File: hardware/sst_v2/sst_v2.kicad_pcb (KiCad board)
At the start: 4 copper layers, 60 x 90 mm, 110 parts, among them U1 Pico_2_W, U2 ADS131M04IPWR, U3 DS3231SN, Y1 ECS-2520MVLC-081.92-BN-TR

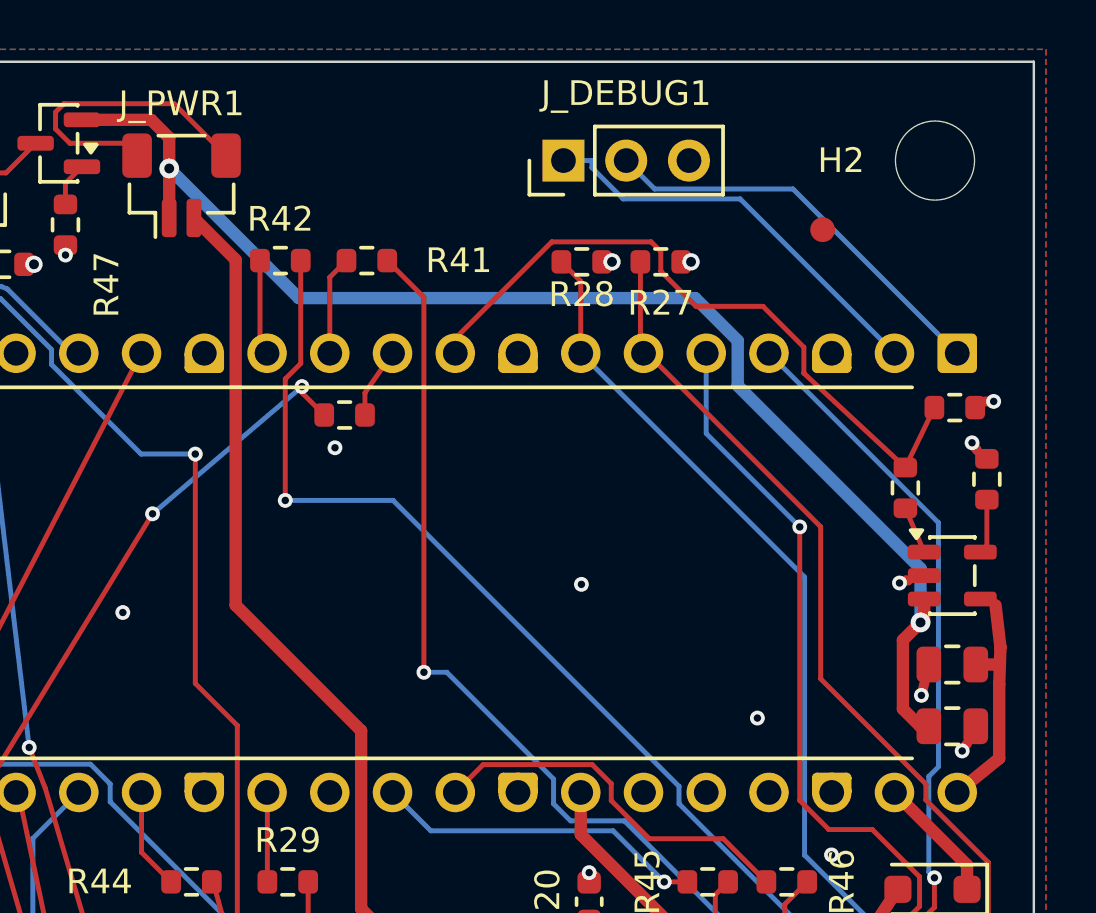
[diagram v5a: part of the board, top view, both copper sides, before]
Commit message: hw: Lader an die Oberkante verlegt, Thermalflaeche an VSS
U_CHG1, C_CHG1/C_CHG2, R_PROG, R_STAT1/R_STAT2 von unter dem Pico nach
x 113-123,6 / y 48,3-55,2 mm (zwischen J_PWR1 und J_DEBUG1). GND-Zone
"Lader Thermal" (F.Cu, Prioritaet 2, volle Anbindung) 0,77 cm2, 6 GND-Vias
0,6/0,3 am VSS-Pad. +VBUS, +VBAT, CHG_STAT neu geroutet, alte Leiterbahnen
und GND-Stichleitungen unter dem Pico entfernt. Courtyard-Ausnahmen der
sechs Teile aus sst_v2.kicad_dru entfernt (R50 bleibt). R42-Referenz
verschoben. Gerber, Bohrdaten, Zip und CPL neu erzeugt.

DRC: 0 Fehler, 0 offene Verbindungen, 0 Paritaetsfehler.

Co-Authored-By: Claude Fable 5.1 <noreply@anthropic.com>
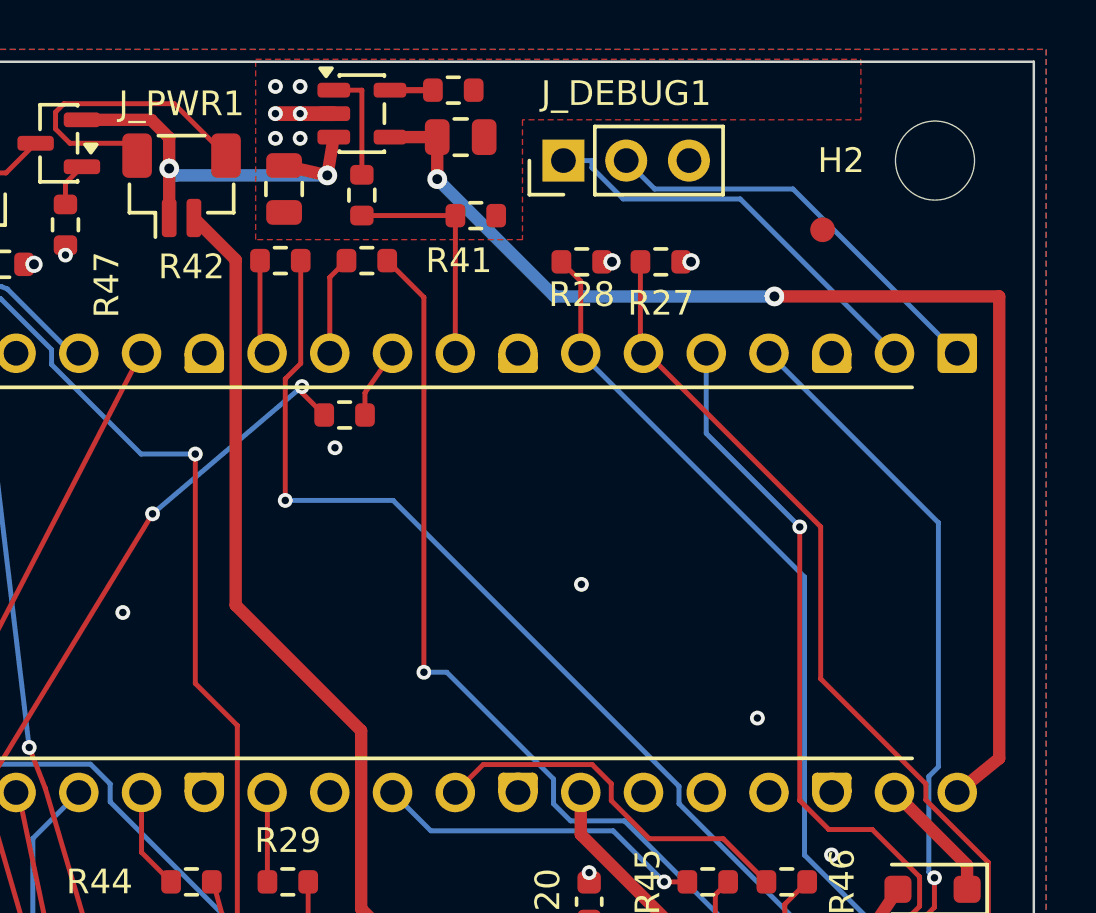
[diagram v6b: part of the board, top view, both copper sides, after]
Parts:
- moved C_CHG2 34.7 mm to (114.2, 53.1), turned to -90 degrees
- moved U_CHG1 30.3 mm to (117.3, 50.1)
- moved C_CHG1 29.2 mm to (121.3, 51.0), turned to 0 degrees
- moved R_PROG 26.7 mm to (121.0, 49.1), turned to 0 degrees
- moved R_STAT1 25.0 mm to (117.3, 53.4), turned to -90 degrees
- moved R_STAT2 20.9 mm to (121.9, 54.2)
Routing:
- net +VBUS: track 9.35 -> 49.2 mm, vias 0 -> 2
- net +VBAT: track 53.7 -> 17.0 mm
- net CHG_STAT: track 27.9 -> 9.36 mm
- net CHG_STAT_5V: track 1.93 -> 4.56 mm
- net GND: track 50.4 -> 50.0 mm, vias 96 -> 97

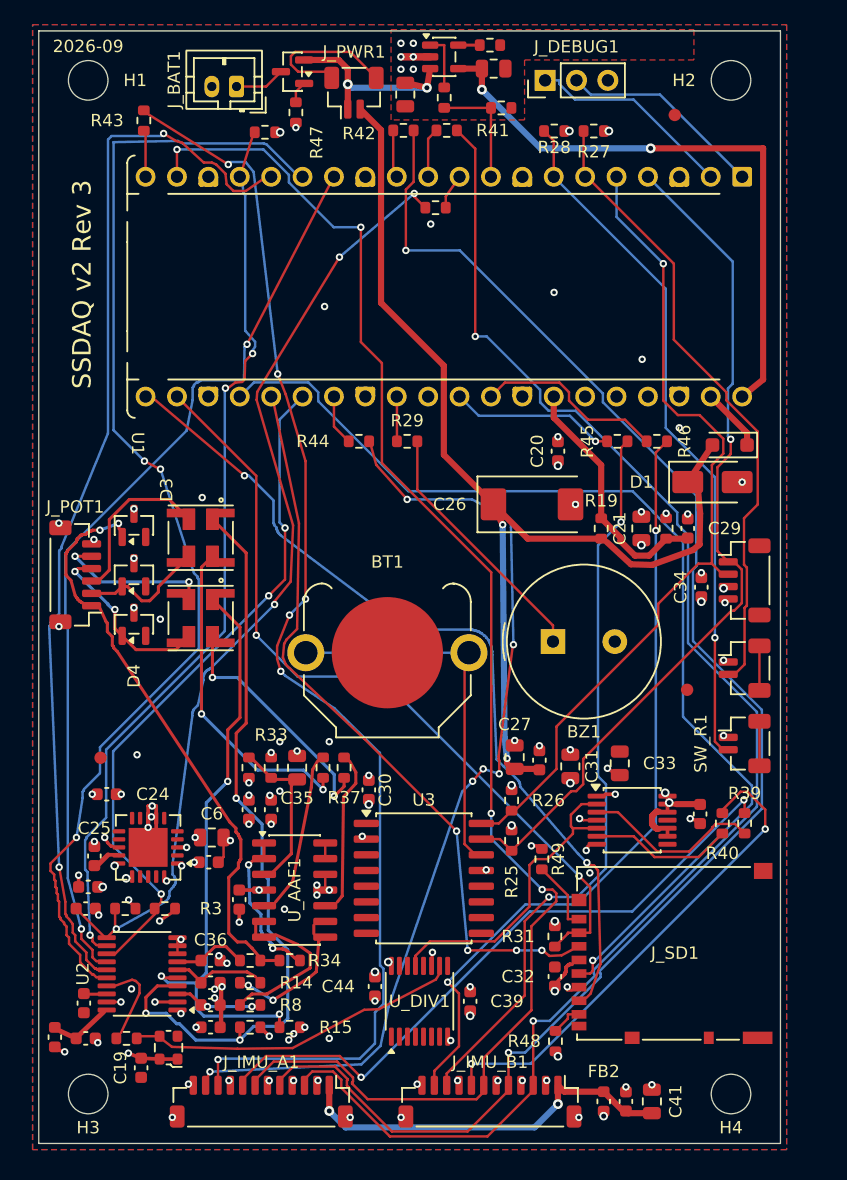
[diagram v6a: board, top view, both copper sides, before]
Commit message: hw: Referenzen 0,8 mm auf Silkscreen, J_DEBUG1/R_STAT1 umgesetzt, Fertigungsdaten neu
Alle Referenzen von Hand positioniert, 0,8 mm Hoehe, 0,15 mm Strich
(PCBWay-Minimum). Ausgeblendete und F.Fab-Referenzen auf F.Silkscreen.
Gerber/Bohrdaten mit --subtract-soldermask, Zip und CPL neu erzeugt.
ERC 0 Fehler, DRC 0 Fehler, 0 offene Verbindungen, 0 Paritaetsfehler.

Co-Authored-By: Claude Opus 5.5 <noreply@anthropic.com>
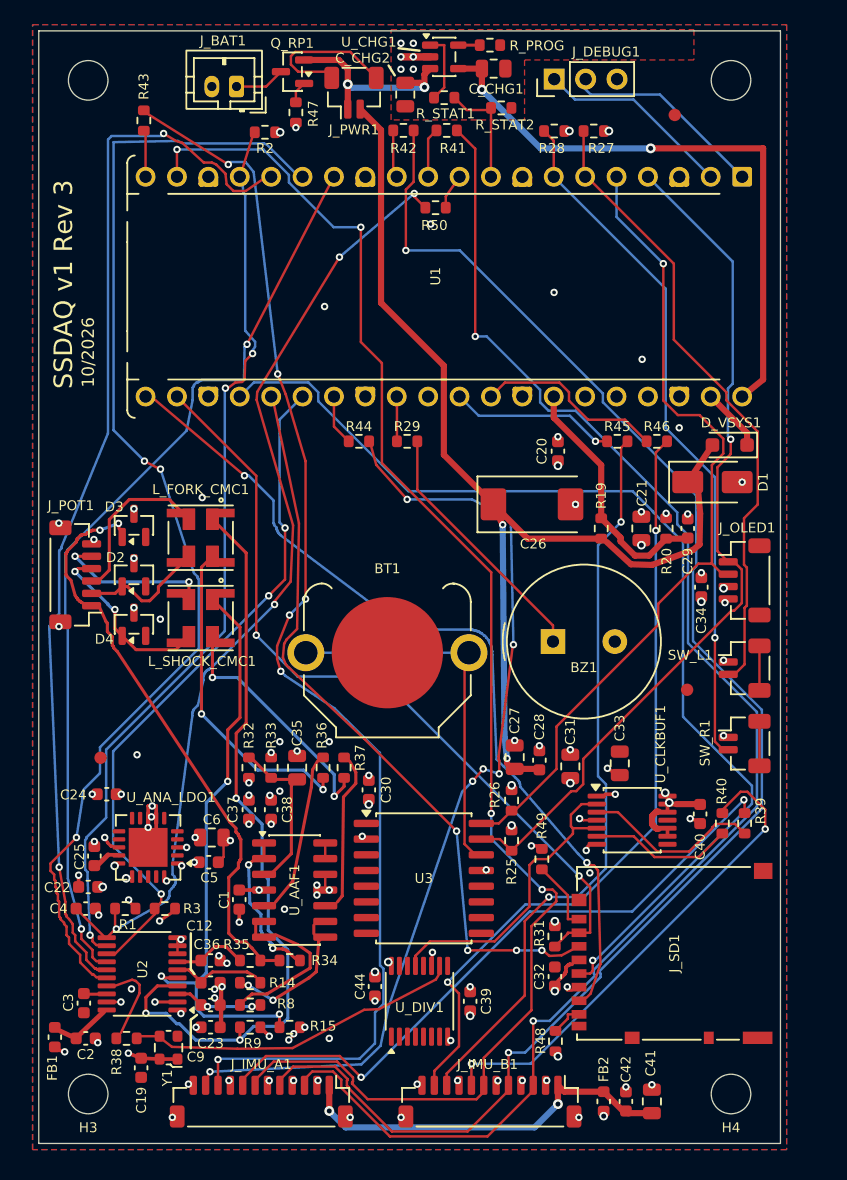
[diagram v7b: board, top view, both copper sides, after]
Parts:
- moved J_DEBUG1 0.75 mm to (126.2, 51.9)
- turned R_STAT1 to 0 degrees
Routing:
- net CHG_STAT_5V: track 4.56 -> 5.73 mm
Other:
- board text added: "10/2026"
- board text added: "SSDAQ v1 Rev 3"
- board text removed: "2026-09"
- board text removed: "SSDAQ v2 Rev 3"
